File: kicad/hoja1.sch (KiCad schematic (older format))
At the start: 1 part

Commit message: creacion bus y libreria
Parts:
- removed U?: STM32F446ZETx, LQFP144, symbol STM32F446ZETx
- added U?: STM32F446ZETx, Housings_QFP:LQFP-144_20x20mm_Pitch0.5mm, symbol STM32F446ZETx
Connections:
- net labels added: FMC[15:0]
- wire segments 0 -> 16
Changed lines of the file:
@@
 LIBS:stm32
 LIBS:Lattice
+LIBS:stm32f446zetx
 LIBS:design_emb-cache
 EELAYER 25 0
@@
 $Comp
 L STM32F446ZETx U?
-U 1 1 5B7DAF5C
-P 16500 8900
-F 0 "U?" H 12000 12625 50  0000 L BNN
-F 1 "STM32F446ZETx" H 21000 12625 50  0000 R BNN
-F 2 "LQFP144" H 21000 12575 50  0001 R TNN
-F 3 "" H 16500 8900 50  0001 C CNN
-	1    16500 8900
+U 1 1 5B7F8688
+P 23700 16600
+F 0 "U?" H 19200 20325 50  0000 L BNN
+F 1 "STM32F446ZETx" H 28200 20325 50  0000 R BNN
+F 2 "Housings_QFP:LQFP-144_20x20mm_Pitch0.5mm" H 28200 20275 50  0001 R TNN
+F 3 "" H 23700 16600 50  0001 C CNN
+	1    23700 16600
 	1    0    0    -1
 $EndComp
+Wire Bus Line
+	18550 19000 18350 19000
+Text HLabel 18350 19000 0    60   Input ~ 0
+FMC[15:0]
+Entry Bus Bus
+	18550 19800 18650 19900
+Entry Bus Bus
+	18550 19700 18650 19800
+Entry Bus Bus
+	18550 19600 18650 19700
+Entry Bus Bus
+	18550 19500 18650 19600
+Entry Bus Bus
+	18550 19400 18650 19500
+Entry Bus Bus
+	18550 19300 18650 19400
+Entry Bus Bus
+	18550 19200 18650 19300
+Entry Bus Bus
+	18550 19100 18650 19200
+Entry Bus Bus
+	18550 19000 18650 19100
+Wire Bus Line
+	18550 19800 18550 19000
+Wire Bus Line
+	28950 18300 29150 18300
+Wire Wire Line
+	28400 19200 28850 19200
+Wire Wire Line
+	28400 19300 28850 19300
+Wire Wire Line
+	28400 19400 28850 19400
+Text HLabel 29150 18300 2    60   Input ~ 0
+FMC[15:0]
+Entry Bus Bus
+	28950 19800 28850 19900
+Entry Bus Bus
+	28950 19700 28850 19800
+Entry Bus Bus
+	28950 19300 28850 19400
+Entry Bus Bus
+	28950 19200 28850 19300
+Entry Bus Bus
+	28950 19100 28850 19200
+Entry Bus Bus
+	28950 18400 28850 18500
+Entry Bus Bus
+	28950 18300 28850 18400
+Wire Wire Line
+	28400 18400 28850 18400
+Wire Wire Line
+	28400 18500 28850 18500
+Wire Wire Line
+	28400 19800 28850 19800
+Wire Wire Line
+	28400 19900 28850 19900
+Wire Bus Line
+	28950 18300 28950 19800
+Wire Wire Line
+	19000 19900 18650 19900
+Wire Wire Line
+	18650 19800 19000 19800
+Wire Wire Line
+	19000 19700 18650 19700
+Wire Wire Line
+	19000 19600 18650 19600
+Wire Wire Line
+	19000 19500 18650 19500
+Wire Wire Line
+	19000 19400 18650 19400
+Wire Wire Line
+	19000 19300 18650 19300
+Wire Wire Line
+	19000 19200 18650 19200
+Wire Wire Line
+	19000 19100 18650 19100
 $EndSCHEMATC

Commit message: creacion bus FMC
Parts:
- removed U?: STM32F446ZETx, Housings_QFP:LQFP-144_20x20mm_Pitch0.5mm, symbol STM32F446ZETx
- added U?: STM32F446ZETx, Package_QFP:LQFP-144_20x20mm_P0.5mm, symbol stm32:STM32F446ZETx
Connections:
- net labels added: FMC_D0, FMC_D1, FMC_D10, FMC_D11, FMC_D12, FMC_D13, FMC_D14, FMC_D15, FMC_D2, FMC_D3, FMC_D4, FMC_D5, FMC_D6, FMC_D7, FMC_D8, FMC_D9
- wire segments 16 -> 0

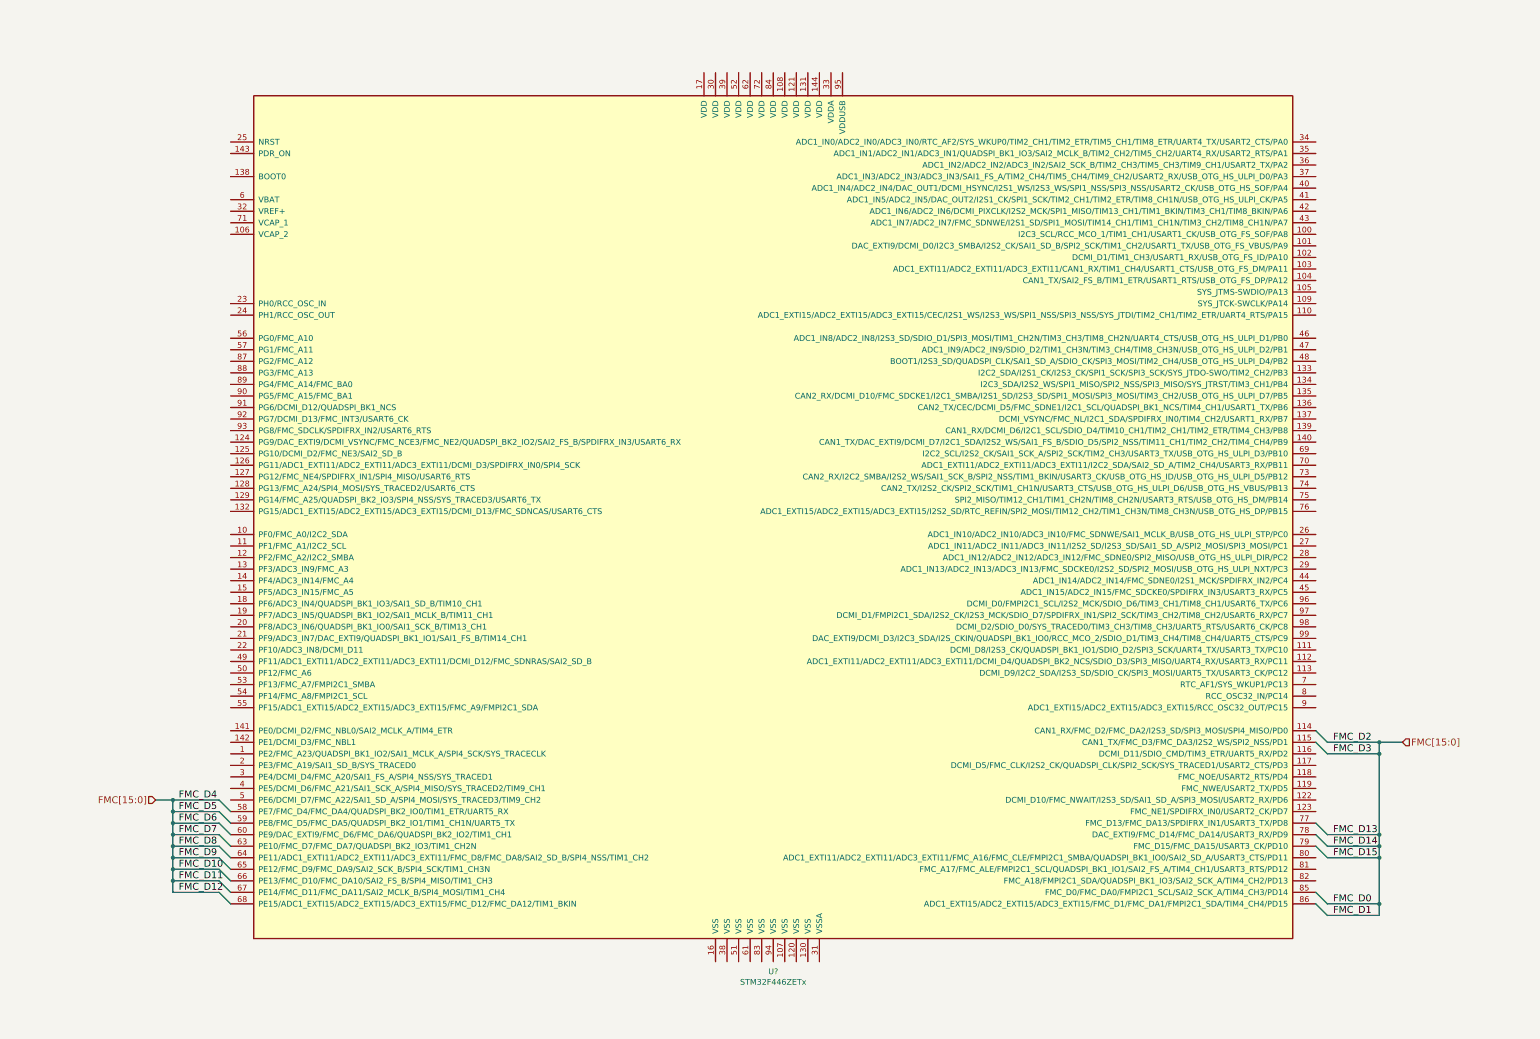
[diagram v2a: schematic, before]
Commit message: creacion buses y alimentacion .sch
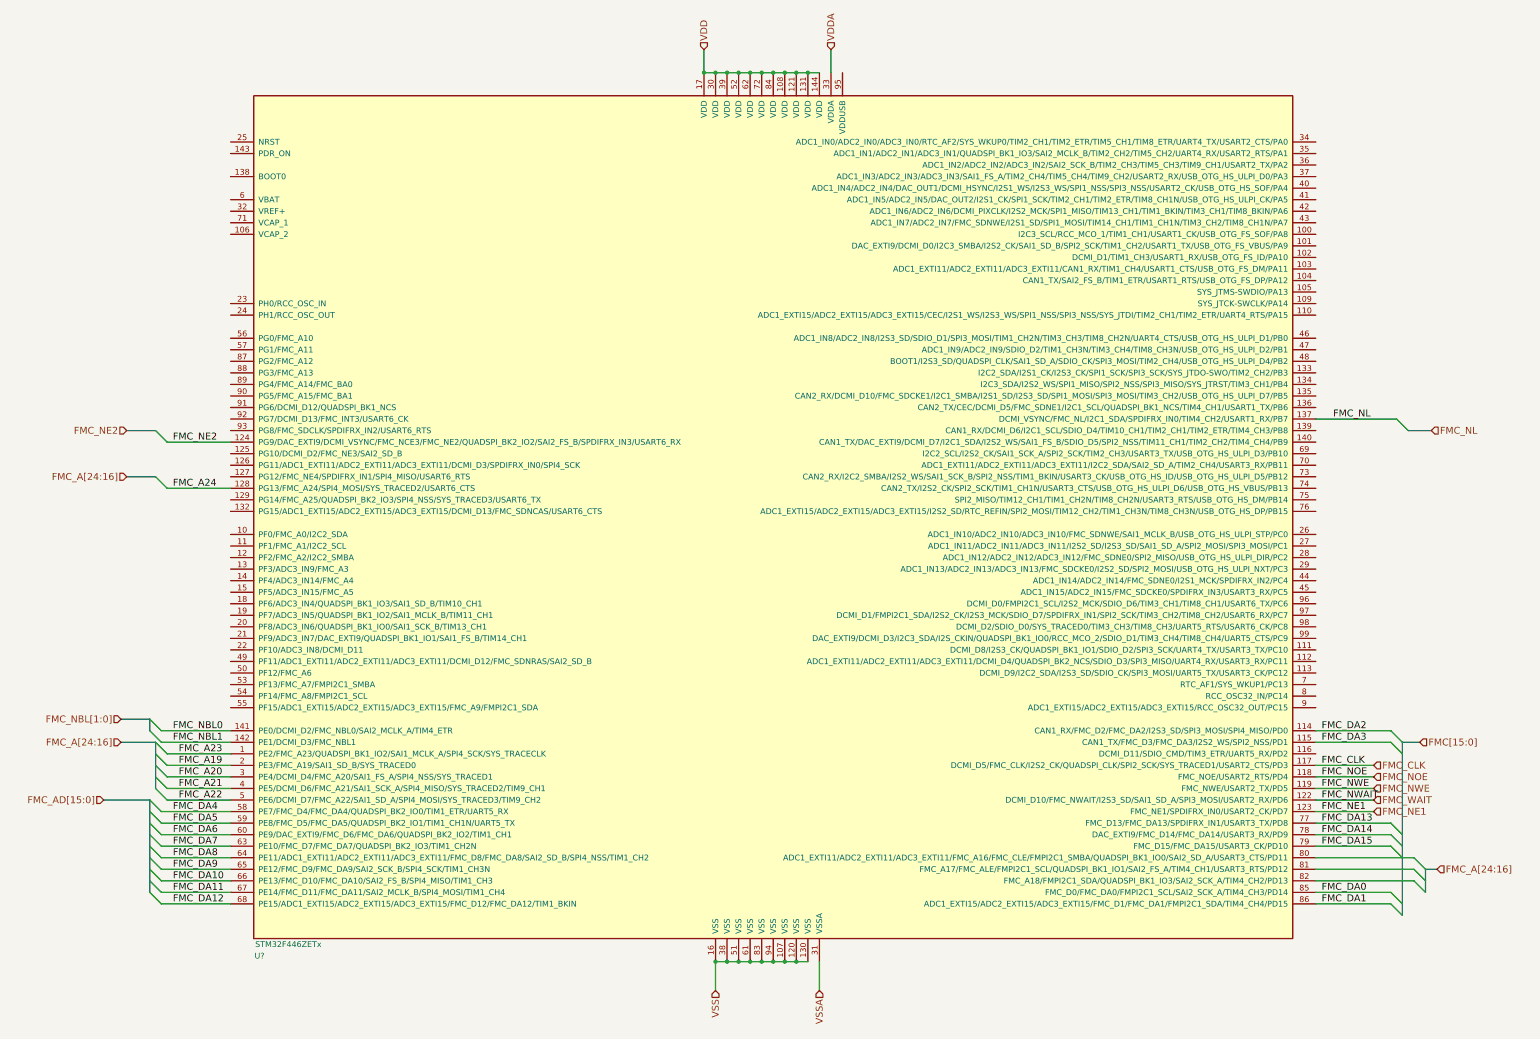
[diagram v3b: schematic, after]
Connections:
- net FMC_A23: now reaches U?.1 (PE2/FMC_A23/QUADSPI_BK1_IO2/SAI1_MCLK_A/SPI4_SCK/SYS_TRACECLK)
- net VSS: now reaches U?.107 (VSS)
- net VSS: now also U?.120 (VSS), U?.130 (VSS), U?.16 (VSS), U?.38 (VSS), U?.51 (VSS), U?.61 (VSS), U?.83 (VSS), U?.94 (VSS)
- net VDD: now reaches U?.108 (VDD)
- net VDD: now also U?.121 (VDD), U?.131 (VDD), U?.144 (VDD), U?.17 (VDD), U?.30 (VDD), U?.39 (VDD), U?.52 (VDD), U?.62 (VDD), U?.72 (VDD), U?.84 (VDD)
- net FMC_DA2: now reaches U?.114 (CAN1_RX/FMC_D2/FMC_DA2/I2S3_SD/SPI3_MOSI/SPI4_MISO/PD0)
- net FMC_DA3: now reaches U?.115 (CAN1_TX/FMC_D3/FMC_DA3/I2S2_WS/SPI2_NSS/PD1)
- net FMC_CLK: now reaches U?.117 (DCMI_D5/FMC_CLK/I2S2_CK/QUADSPI_CLK/SPI2_SCK/SYS_TRACED1/USART2_CTS/PD3)
- net FMC_NOE: now reaches U?.118 (FMC_NOE/USART2_RTS/PD4)
- net FMC_NWE: now reaches U?.119 (FMC_NWE/USART2_TX/PD5)
- net FMC_WAIT: now reaches U?.122 (DCMI_D10/FMC_NWAIT/I2S3_SD/SAI1_SD_A/SPI3_MOSI/USART2_RX/PD6)
- net FMC_NE1: now reaches U?.123 (FMC_NE1/SPDIFRX_IN0/USART2_CK/PD7)
- net FMC_NE2: now reaches U?.124 (PG9/DAC_EXTI9/DCMI_VSYNC/FMC_NCE3/FMC_NE2/QUADSPI_BK2_IO2/SAI2_FS_B/SPDIFRX_IN3/USART6_RX)
- net FMC_A24: now reaches U?.128 (PG13/FMC_A24/SPI4_MOSI/SYS_TRACED2/USART6_CTS)
- net FMC_NL: now reaches U?.137 (DCMI_VSYNC/FMC_NL/I2C1_SDA/SPDIFRX_IN0/TIM4_CH2/USART1_RX/PB7)
- net FMC_NBL0: now reaches U?.141 (PE0/DCMI_D2/FMC_NBL0/SAI2_MCLK_A/TIM4_ETR)
- net FMC_NBL1: now reaches U?.142 (PE1/DCMI_D3/FMC_NBL1)
- net FMC_A19: now reaches U?.2 (PE3/FMC_A19/SAI1_SD_B/SYS_TRACED0)
- net FMC_A20: now reaches U?.3 (PE4/DCMI_D4/FMC_A20/SAI1_FS_A/SPI4_NSS/SYS_TRACED1)
- net VSSA: now reaches U?.31 (VSSA)
- net VDDA: now reaches U?.33 (VDDA)
- net FMC_A21: now reaches U?.4 (PE5/DCMI_D6/FMC_A21/SAI1_SCK_A/SPI4_MISO/SYS_TRACED2/TIM9_CH1)
- net FMC_A22: now reaches U?.5 (PE6/DCMI_D7/FMC_A22/SAI1_SD_A/SPI4_MOSI/SYS_TRACED3/TIM9_CH2)
- net FMC_DA4: now reaches U?.58 (PE7/FMC_D4/FMC_DA4/QUADSPI_BK2_IO0/TIM1_ETR/UART5_RX)
- net FMC_DA5: now reaches U?.59 (PE8/FMC_D5/FMC_DA5/QUADSPI_BK2_IO1/TIM1_CH1N/UART5_TX)
- net FMC_DA6: now reaches U?.60 (PE9/DAC_EXTI9/FMC_D6/FMC_DA6/QUADSPI_BK2_IO2/TIM1_CH1)
- net FMC_DA7: now reaches U?.63 (PE10/FMC_D7/FMC_DA7/QUADSPI_BK2_IO3/TIM1_CH2N)
- net FMC_DA8: now reaches U?.64 (PE11/ADC1_EXTI11/ADC2_EXTI11/ADC3_EXTI11/FMC_D8/FMC_DA8/SAI2_SD_B/SPI4_NSS/TIM1_CH2)
- net FMC_DA9: now reaches U?.65 (PE12/FMC_D9/FMC_DA9/SAI2_SCK_B/SPI4_SCK/TIM1_CH3N)
- net FMC_DA10: now reaches U?.66 (PE13/FMC_D10/FMC_DA10/SAI2_FS_B/SPI4_MISO/TIM1_CH3)
- net FMC_DA11: now reaches U?.67 (PE14/FMC_D11/FMC_DA11/SAI2_MCLK_B/SPI4_MOSI/TIM1_CH4)
- net FMC_DA12: now reaches U?.68 (PE15/ADC1_EXTI15/ADC2_EXTI15/ADC3_EXTI15/FMC_D12/FMC_DA12/TIM1_BKIN)
- net FMC_DA13: now reaches U?.77 (FMC_D13/FMC_DA13/SPDIFRX_IN1/USART3_TX/PD8)
- net FMC_DA14: now reaches U?.78 (DAC_EXTI9/FMC_D14/FMC_DA14/USART3_RX/PD9)
- net FMC_DA15: now reaches U?.79 (FMC_D15/FMC_DA15/USART3_CK/PD10)
- net FMC_DA0: now reaches U?.85 (FMC_D0/FMC_DA0/FMPI2C1_SCL/SAI2_SCK_A/TIM4_CH3/PD14)
- net FMC_DA1: now reaches U?.86 (ADC1_EXTI15/ADC2_EXTI15/ADC3_EXTI15/FMC_D1/FMC_DA1/FMPI2C1_SDA/TIM4_CH4/PD15)
